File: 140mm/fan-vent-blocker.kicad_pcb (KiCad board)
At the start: 2 copper layers, 140 x 140 mm, 5 parts

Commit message: New gerbers
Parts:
- added G***: LOGO, locallib:ai-ring-small-mask, B.Cu at (45.0, 155.0)
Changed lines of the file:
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@@
     (tracks 0)
     (zones 0)
-    (modules 5)
+    (modules 6)
     (nets 2)
   )
@@
     (add_net GND)
   )
+  (module locallib:ai-ring-small-mask (layer B.Cu)
+    (at 45 155 180)
+    (fp_text reference G*** (at 0 0) (layer Dwgs.User) hide
+      (effects (font (size 1.524 1.524) (thickness 0.3)))
+    )
+    (fp_text value LOGO (at 0.75 0) (layer Dwgs.User) hide
+      (effects (font (size 1.524 1.524) (thickness 0.3)))
+    )
+    (fp_poly (pts (xy 0.1905 1.0795) (xy -0.214312 1.0795) (xy -0.214312 1.484312) (xy 0.1905 1.484312)
+      (xy 0.1905 1.0795)) (layer B.Mask) (width 0.01))
+    (fp_poly (pts (xy 0.595313 0.293687) (xy 0.1905 0.293687) (xy 0.1905 0.674687) (xy 0.595313 0.674687)
+      (xy 0.595313 0.293687)) (layer B.Mask) (width 0.01))
+    (fp_poly (pts (xy -0.214312 0.293687) (xy -0.595312 0.293687) (xy -0.595312 0.674687) (xy -0.214312 0.674687)
+      (xy -0.214312 0.293687)) (layer B.Mask) (width 0.01))
+    (fp_poly (pts (xy 0.976313 -0.515938) (xy 0.595313 -0.515938) (xy 0.595313 -0.111125) (xy 0.976313 -0.111125)
+      (xy 0.976313 -0.515938)) (layer B.Mask) (width 0.01))
+    (fp_poly (pts (xy 0.1905 -0.515938) (xy -0.214312 -0.515938) (xy -0.214312 -0.111125) (xy 0.1905 -0.111125)
+      (xy 0.1905 -0.515938)) (layer B.Mask) (width 0.01))
+    (fp_poly (pts (xy -0.595312 -0.515938) (xy -1.000125 -0.515938) (xy -1.000125 -0.111125) (xy -0.595312 -0.111125)
+      (xy -0.595312 -0.515938)) (layer B.Mask) (width 0.01))
+    (fp_poly (pts (xy 1.381125 -1.30175) (xy 0.976313 -1.30175) (xy 0.976313 -0.896938) (xy 1.381125 -0.896938)
+      (xy 1.381125 -1.30175)) (layer B.Mask) (width 0.01))
+    (fp_poly (pts (xy -1.000125 -1.30175) (xy -1.404937 -1.30175) (xy -1.404937 -0.896938) (xy -1.000125 -0.896938)
+      (xy -1.000125 -1.30175)) (layer B.Mask) (width 0.01))
+    (fp_poly (pts (xy 0.003969 2.971955) (xy 0.128087 2.970585) (xy 0.239799 2.966428) (xy 0.342392 2.959081)
+      (xy 0.439156 2.94814) (xy 0.533378 2.933202) (xy 0.628347 2.913863) (xy 0.727351 2.889719)
+      (xy 0.77263 2.877582) (xy 0.981177 2.812344) (xy 1.183265 2.733008) (xy 1.378128 2.639972)
+      (xy 1.564999 2.533632) (xy 1.743114 2.414384) (xy 1.89526 2.296383) (xy 2.052928 2.155658)
+      (xy 2.200265 2.004213) (xy 2.336586 1.843115) (xy 2.461208 1.673433) (xy 2.573447 1.496234)
+      (xy 2.67262 1.312584) (xy 2.758042 1.123553) (xy 2.82903 0.930207) (xy 2.877784 0.762197)
+      (xy 2.910855 0.622211) (xy 2.936215 0.490275) (xy 2.954607 0.361003) (xy 2.966775 0.229007)
+      (xy 2.973461 0.0889) (xy 2.974114 0.0635) (xy 2.971395 -0.154797) (xy 2.9532 -0.36958)
+      (xy 2.919535 -0.580821) (xy 2.870406 -0.788489) (xy 2.805819 -0.992555) (xy 2.741622 -1.156487)
+      (xy 2.713539 -1.221752) (xy 2.689477 -1.27591) (xy 2.667608 -1.322613) (xy 2.646107 -1.365513)
+      (xy 2.623146 -1.408263) (xy 2.5969 -1.454515) (xy 2.567775 -1.504156) (xy 2.448556 -1.690427)
+      (xy 2.318452 -1.865153) (xy 2.177329 -2.028465) (xy 2.025055 -2.180496) (xy 1.861497 -2.32138)
+      (xy 1.686524 -2.451248) (xy 1.504156 -2.567775) (xy 1.451327 -2.598744) (xy 1.405414 -2.624721)
+      (xy 1.362765 -2.647531) (xy 1.319728 -2.669001) (xy 1.272651 -2.690957) (xy 1.217881 -2.715225)
+      (xy 1.156487 -2.741622) (xy 1.060254 -2.781169) (xy 0.971536 -2.814208) (xy 0.884422 -2.842695)
+      (xy 0.792998 -2.868589) (xy 0.710406 -2.889322) (xy 0.54589 -2.924876) (xy 0.388795 -2.950553)
+      (xy 0.234567 -2.966893) (xy 0.078649 -2.974436) (xy -0.011906 -2.975013) (xy -0.063125 -2.974498)
+      (xy -0.111246 -2.973793) (xy -0.153126 -2.97296) (xy -0.185622 -2.972063) (xy -0.20559 -2.971165)
+      (xy -0.206375 -2.971109) (xy -0.422549 -2.947157) (xy -0.635306 -2.90817) (xy -0.843787 -2.854467)
+      (xy -1.047132 -2.786363) (xy -1.244484 -2.704176) (xy -1.434982 -2.608225) (xy -1.617768 -2.498826)
+      (xy -1.768724 -2.393796) (xy -1.941651 -2.255449) (xy -2.102335 -2.107088) (xy -2.250549 -1.949039)
+      (xy -2.386071 -1.781632) (xy -2.508676 -1.605194) (xy -2.618139 -1.420052) (xy -2.714237 -1.226535)
+      (xy -2.796744 -1.024971) (xy -2.865437 -0.815688) (xy -2.877582 -0.77263) (xy -2.903948 -0.670835)
+      (xy -2.925333 -0.574511) (xy -2.942141 -0.480367) (xy -2.954775 -0.385117) (xy -2.96364 -0.28547)
+      (xy -2.969138 -0.17814) (xy -2.971674 -0.059836) (xy -2.971955 -0.003969) (xy -2.97128 0.051392)
+      (xy -2.439206 0.051392) (xy -2.439103 -0.028746) (xy -2.437437 -0.10841) (xy -2.434241 -0.183537)
+      (xy -2.429544 -0.25006) (xy -2.425824 -0.28575) (xy -2.39395 -0.483048) (xy -2.347299 -0.674663)
+      (xy -2.286049 -0.860222) (xy -2.210381 -1.039349) (xy -2.120473 -1.211669) (xy -2.016506 -1.376809)
+      (xy -1.898659 -1.534393) (xy -1.767112 -1.684047) (xy -1.744776 -1.70726) (xy -1.610542 -1.834334)
+      (xy -1.46484 -1.95227) (xy -1.310369 -2.05909) (xy -1.149831 -2.152816) (xy -1.104042 -2.176504)
+      (xy -1.029634 -2.213153) (xy -0.964393 -2.243372) (xy -0.903896 -2.26894) (xy -0.843722 -2.291634)
+      (xy -0.779449 -2.313233) (xy -0.714375 -2.333227) (xy -0.525162 -2.38264) (xy -0.339411 -2.417091)
+      (xy -0.155673 -2.436714) (xy 0.027503 -2.441642) (xy 0.211564 -2.432011) (xy 0.278106 -2.425031)
+      (xy 0.465438 -2.396087) (xy 0.645019 -2.354278) (xy 0.819357 -2.298854) (xy 0.990959 -2.229064)
+      (xy 1.087916 -2.182866) (xy 1.258548 -2.089447) (xy 1.417964 -1.985712) (xy 1.566922 -1.870974)
+      (xy 1.706179 -1.74455) (xy 1.836494 -1.605754) (xy 1.958624 -1.453903) (xy 2.066892 -1.298259)
+      (xy 2.092018 -1.257068) (xy 2.121341 -1.20494) (xy 2.153041 -1.145496) (xy 2.185299 -1.082356)
+      (xy 2.216293 -1.01914) (xy 2.244206 -0.959467) (xy 2.267215 -0.906957) (xy 2.280653 -0.873125)
+      (xy 2.34352 -0.681584) (xy 2.390916 -0.488845) (xy 2.4228 -0.29545) (xy 2.43913 -0.10194)
+      (xy 2.439868 0.091143) (xy 2.424972 0.283258) (xy 2.394402 0.473864) (xy 2.384599 0.519906)
+      (xy 2.35095 0.656199) (xy 2.312642 0.782382) (xy 2.267704 0.903993) (xy 2.214163 1.026568)
+      (xy 2.176504 1.104042) (xy 2.082799 1.27289) (xy 1.975974 1.433327) (xy 1.856798 1.584632)
+      (xy 1.726037 1.726086) (xy 1.58446 1.856969) (xy 1.432834 1.97656) (xy 1.271927 2.08414)
+      (xy 1.102507 2.178989) (xy 0.958325 2.24652) (xy 0.786697 2.312915) (xy 0.614143 2.364913)
+      (xy 0.438656 2.402922) (xy 0.258226 2.427349) (xy 0.070845 2.438603) (xy 0.007938 2.439493)
+      (xy -0.190157 2.433123) (xy -0.381785 2.412478) (xy -0.567719 2.377327) (xy -0.748735 2.327433)
+      (xy -0.925606 2.262565) (xy -1.099106 2.182487) (xy -1.270009 2.086965) (xy -1.370706 2.022756)
+      (xy -1.510139 1.921228) (xy -1.644337 1.806722) (xy -1.771659 1.681161) (xy -1.890465 1.546469)
+      (xy -1.999114 1.404569) (xy -2.095965 1.257385) (xy -2.179378 1.106839) (xy -2.214174 1.03392)
+      (xy -2.275577 0.889061) (xy -2.325808 0.749822) (xy -2.366065 0.611874) (xy -2.397544 0.470886)
+      (xy -2.421444 0.322529) (xy -2.429845 0.254) (xy -2.434608 0.19683) (xy -2.437718 0.127939)
+      (xy -2.439206 0.051392) (xy -2.97128 0.051392) (xy -2.97021 0.139027) (xy -2.964336 0.269894)
+      (xy -2.953762 0.391975) (xy -2.937915 0.508615) (xy -2.916223 0.623156) (xy -2.888113 0.738941)
+      (xy -2.853014 0.859313) (xy -2.810353 0.987616) (xy -2.794659 1.031875) (xy -2.716274 1.226594)
+      (xy -2.623434 1.414928) (xy -2.516328 1.596615) (xy -2.395148 1.771392) (xy -2.260083 1.938997)
+      (xy -2.111326 2.099167) (xy -1.949067 2.25164) (xy -1.842229 2.341821) (xy -1.7564 2.407314)
+      (xy -1.658861 2.47464) (xy -1.553252 2.541588) (xy -1.443214 2.605945) (xy -1.332387 2.6655)
+      (xy -1.224411 2.718042) (xy -1.218406 2.720785) (xy -1.148446 2.750658) (xy -1.067265 2.782044)
+      (xy -0.979233 2.813464) (xy -0.888721 2.843438) (xy -0.800099 2.870489) (xy -0.717736 2.893136)
+      (xy -0.68585 2.901029) (xy -0.592625 2.921797) (xy -0.503651 2.938457) (xy -0.415647 2.951348)
+      (xy -0.325331 2.960805) (xy -0.229422 2.967168) (xy -0.12464 2.970772) (xy -0.007705 2.971956)
+      (xy 0.003969 2.971955)) (layer B.Mask) (width 0.01))
+  )
   (module locallib:ai-ring-25mm-mask (layer F.Cu)

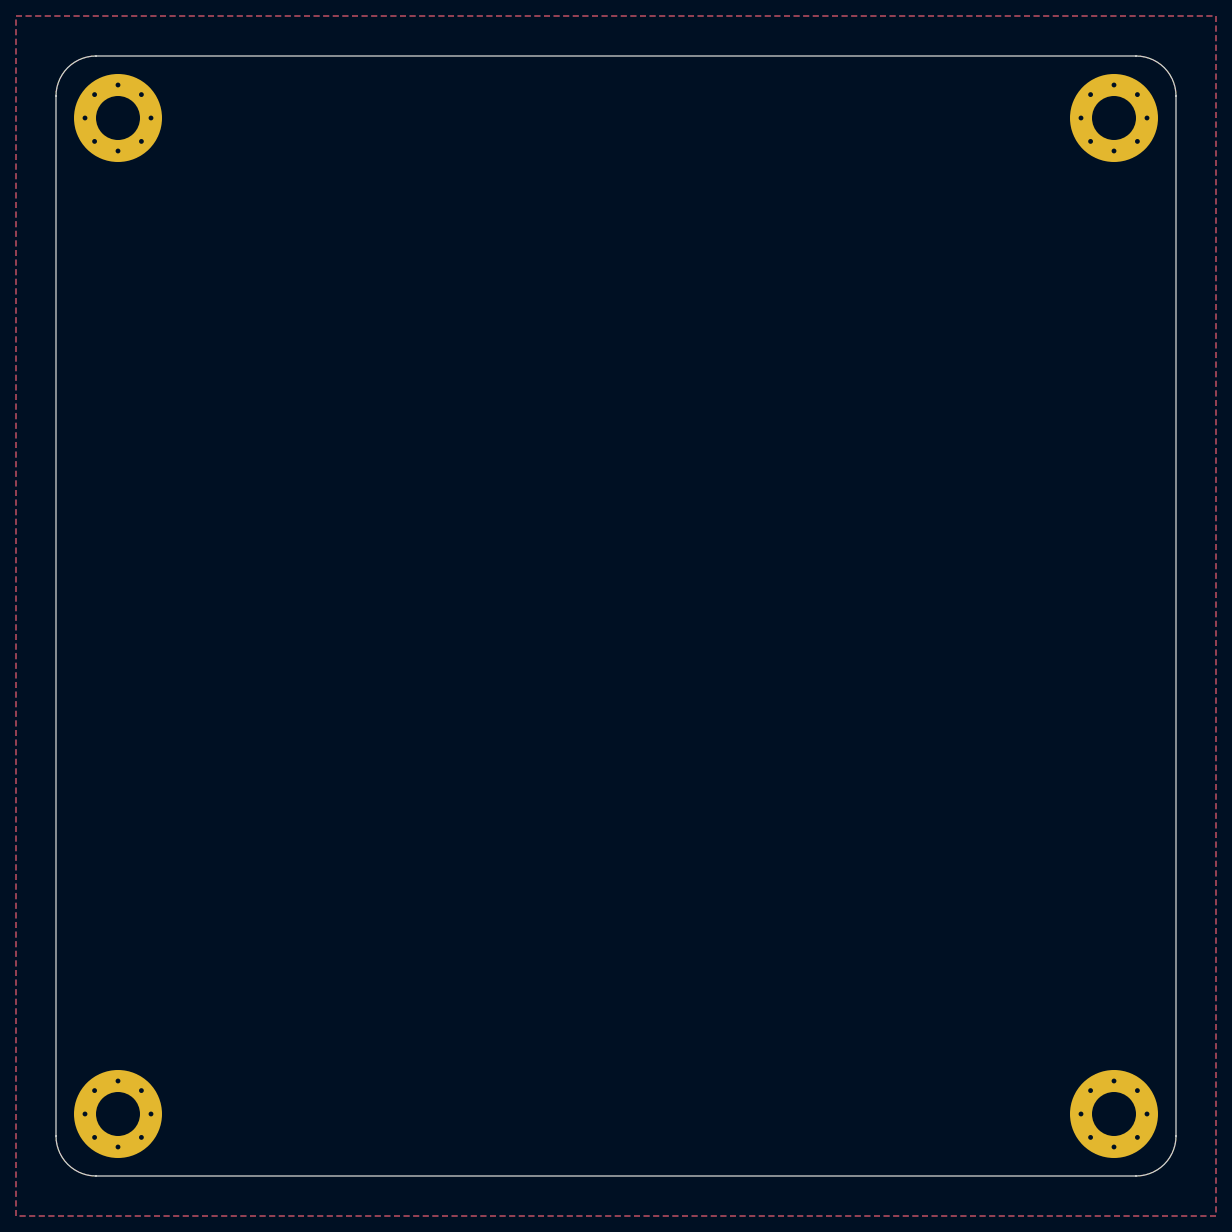
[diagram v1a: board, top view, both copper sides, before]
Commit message: Update to M4 mounting hardware
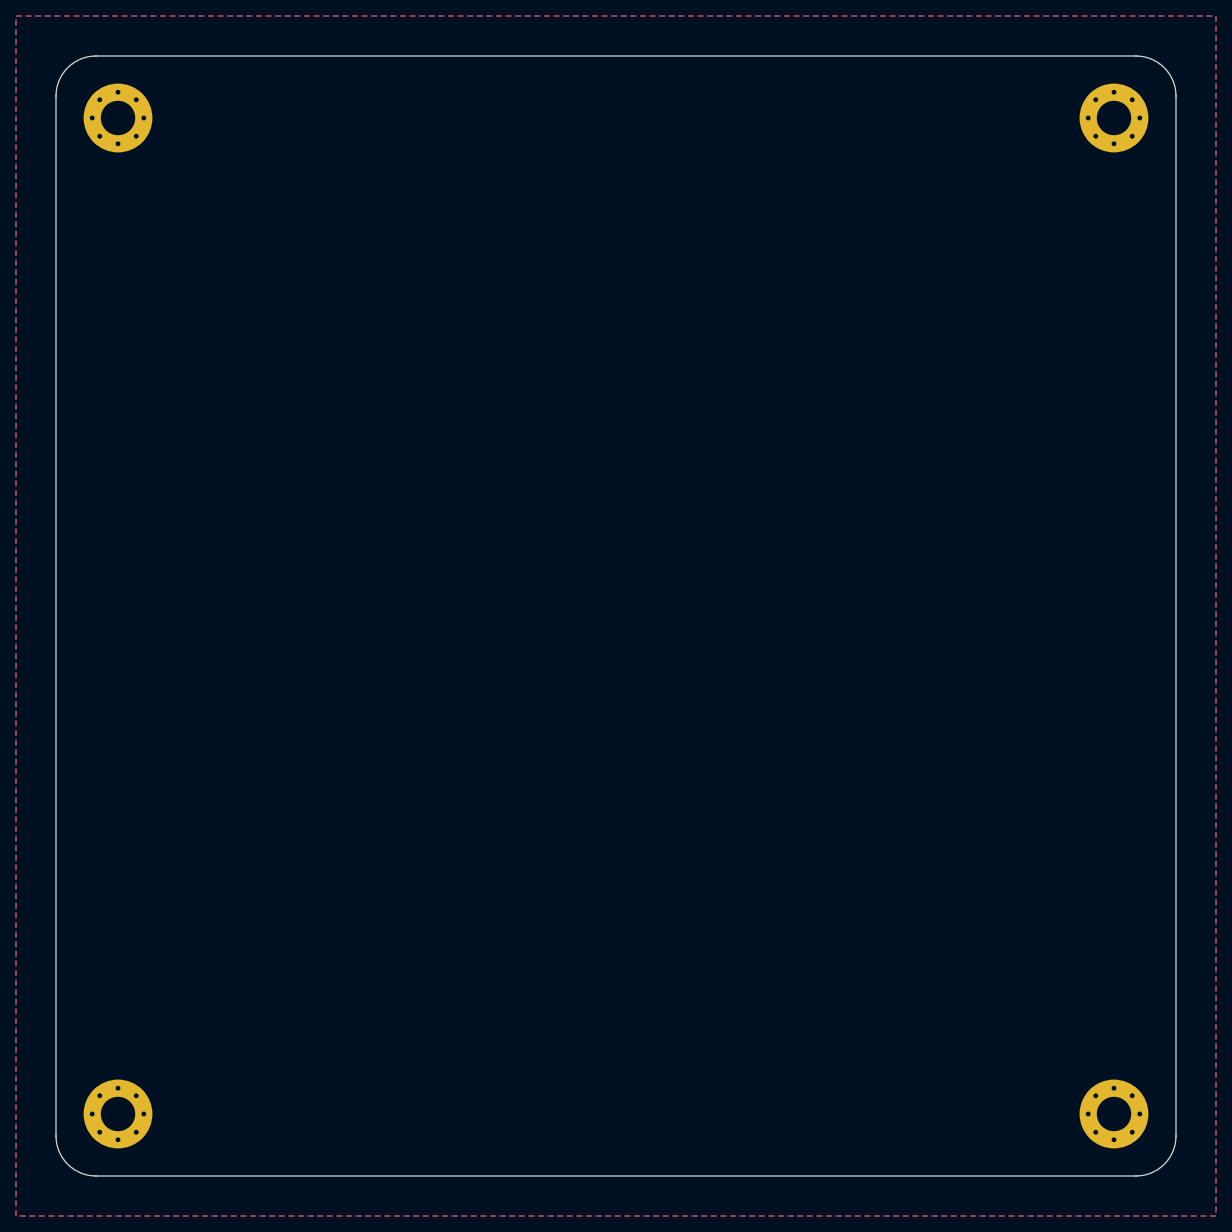
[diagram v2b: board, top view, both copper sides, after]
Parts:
- MH1, MH2, MH3, MH4: footprint locallib:MountingHole_5.5mm_Pad_Via -> MountingHole:MountingHole_4.3mm_M4_Pad_Via
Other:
- board text added: "140mm Fan Vent Blocker | www.ai03.com"
- board text removed: "140mm Fan Vent Blocker | www.ai03.me"
